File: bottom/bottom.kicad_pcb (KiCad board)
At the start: 2 copper layers, 27.5 x 37.7 mm, 0 parts

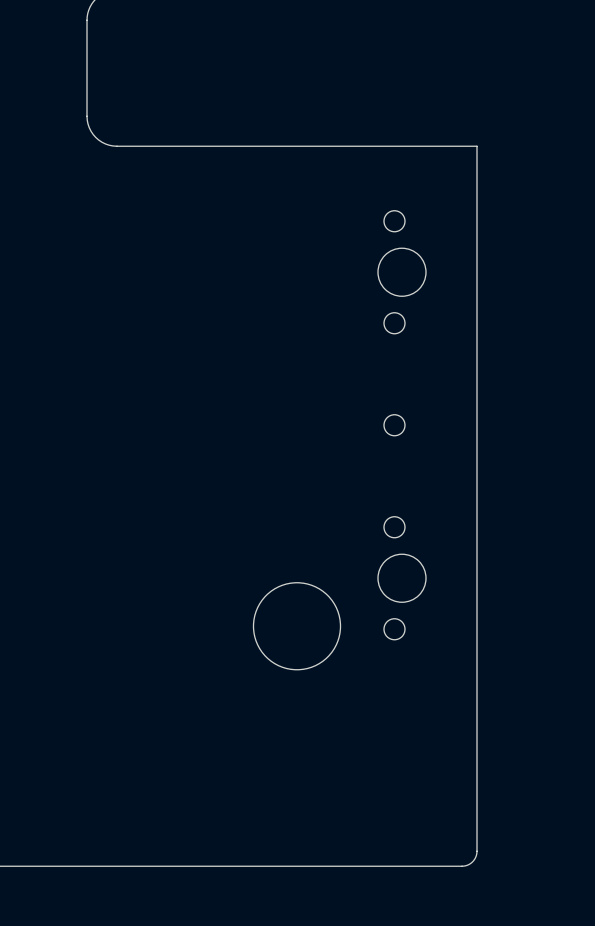
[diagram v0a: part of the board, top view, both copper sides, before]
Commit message: Add pogo pin connector.
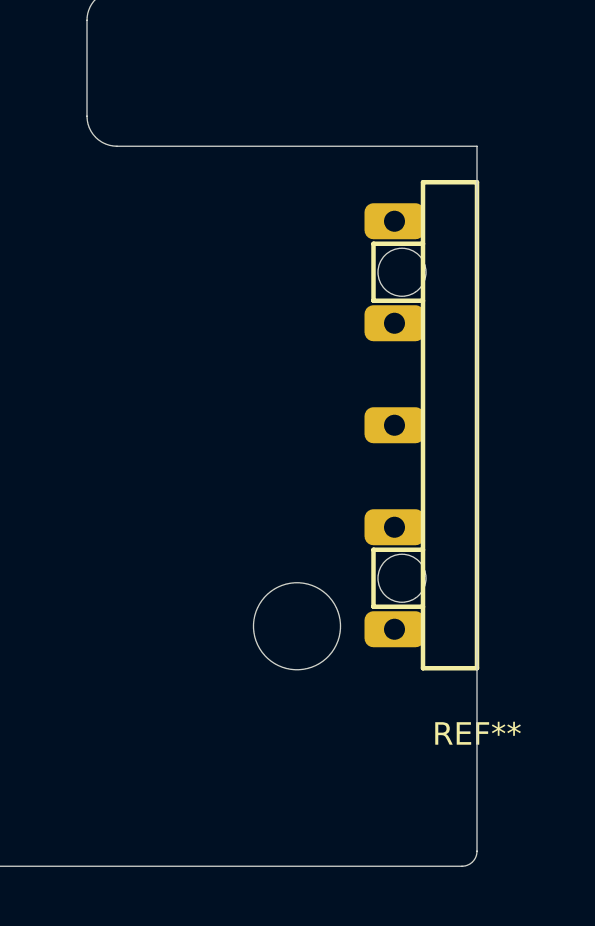
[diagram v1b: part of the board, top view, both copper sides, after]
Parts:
- added REF**: VAL**, ugl:UHK_Male_Pogo_Pin_v2, F.Cu at (225.3, 143.1)
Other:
- outline, holes or cut-outs redrawn
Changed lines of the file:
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@@
   (general
     (thickness 1.6)
-    (drawings 39)
+    (drawings 32)
     (tracks 0)
     (zones 0)
-    (modules 0)
+    (modules 1)
     (nets 1)
   )
@@
     (uvia_drill 0.127)
   )
+  (module ugl:UHK_Male_Pogo_Pin_v2 (layer F.Cu)
+    (at 225.35 143.139999)
+    (attr virtual)
+    (fp_text reference REF** (at 0 10.3) (layer F.SilkS)
+      (effects (font (size 0.75 0.75) (thickness 0.15)))
+    )
+    (fp_text value VAL** (at 0 -9.95 180) (layer F.SilkS) hide
+      (effects (font (size 0.75 0.75) (thickness 0.15)))
+    )
+    (fp_line (start 2.5 -9.1) (end 2.5 9.3) (layer Cmts.User) (width 0.15))
+    (fp_line (start 0 9.3) (end 2.5 9.3) (layer Cmts.User) (width 0.15))
+    (fp_line (start -1.8 8.1) (end -1.8 -8.1) (layer F.SilkS) (width 0.15))
+    (fp_line (start 0 -9.1) (end 2.5 -9.1) (layer Cmts.User) (width 0.15))
+    (fp_line (start 2.5 -7.3) (end 3 -7.3) (layer Cmts.User) (width 0.15))
+    (fp_line (start 2.5 -6.3) (end 3 -6.3) (layer Cmts.User) (width 0.15))
+    (fp_arc (start 3.1 -6.8) (end 3.1 -6.3) (angle -180) (layer Cmts.User) (width 0.15))
+    (fp_line (start 2.5 -2.9) (end 3 -2.9) (layer Cmts.User) (width 0.15))
+    (fp_line (start 2.5 -3.9) (end 3 -3.9) (layer Cmts.User) (width 0.15))
+    (fp_arc (start 3.1 -3.4) (end 3.1 -2.9) (angle -180) (layer Cmts.User) (width 0.15))
+    (fp_line (start 2.5 0.5) (end 3 0.5) (layer Cmts.User) (width 0.15))
+    (fp_line (start 2.5 -0.5) (end 3 -0.5) (layer Cmts.User) (width 0.15))
+    (fp_arc (start 3.1 0) (end 3.1 0.5) (angle -180) (layer Cmts.User) (width 0.15))
+    (fp_line (start 2.5 3.9) (end 3 3.9) (layer Cmts.User) (width 0.15))
+    (fp_line (start 2.5 2.9) (end 3 2.9) (layer Cmts.User) (width 0.15))
+    (fp_arc (start 3.1 3.4) (end 3.1 3.9) (angle -180) (layer Cmts.User) (width 0.15))
+    (fp_line (start 2.5 7.3) (end 3 7.3) (layer Cmts.User) (width 0.15))
+    (fp_line (start 2.5 6.3) (end 3 6.3) (layer Cmts.User) (width 0.15))
+    (fp_arc (start 3.1 6.8) (end 3.1 7.3) (angle -180) (layer Cmts.User) (width 0.15))
+    (fp_line (start 0 9.3) (end 0 -9.1) (layer Cmts.User) (width 0.15))
+    (fp_line (start -1.8 -8.1) (end 0 -8.1) (layer F.SilkS) (width 0.15))
+    (fp_line (start 0 8.1) (end -1.8 8.1) (layer F.SilkS) (width 0.15))
+    (fp_line (start -1.8 -6.05) (end -3.45 -6.05) (layer F.SilkS) (width 0.15))
+    (fp_line (start -3.45 -6.05) (end -3.45 -4.15) (layer F.SilkS) (width 0.15))
+    (fp_line (start -3.45 -4.15) (end -1.8 -4.15) (layer F.SilkS) (width 0.15))
+    (fp_line (start -1.8 6.05) (end -3.45 6.05) (layer F.SilkS) (width 0.15))
+    (fp_line (start -3.45 6.05) (end -3.45 4.15) (layer F.SilkS) (width 0.15))
+    (fp_line (start -3.45 4.15) (end -1.8 4.15) (layer F.SilkS) (width 0.15))
+    (fp_line (start 0 8.1) (end 0 -8.1) (layer F.SilkS) (width 0.15))
+    (pad 1 thru_hole roundrect (at -2.75 -6.8) (size 2 1.2) (drill 0.7) (layers *.Cu *.Mask) (roundrect_rratio 0.25)
+      (clearance 0.0762))
+    (pad 2 thru_hole roundrect (at -2.75 -3.4) (size 2 1.2) (drill 0.7) (layers *.Cu *.Mask) (roundrect_rratio 0.25)
+      (clearance 0.0762))
+    (pad 3 thru_hole roundrect (at -2.75 0) (size 2 1.2) (drill 0.7) (layers *.Cu *.Mask) (roundrect_rratio 0.25))
+    (pad 4 thru_hole roundrect (at -2.75 3.4) (size 2 1.2) (drill 0.7) (layers *.Cu *.Mask) (roundrect_rratio 0.25)
+      (clearance 0.0762))
+    (pad 5 thru_hole roundrect (at -2.75 6.8) (size 2 1.2) (drill 0.7) (layers *.Cu *.Mask) (roundrect_rratio 0.25)
+      (clearance 0.0762))
+    (pad "" np_thru_hole circle (at -2.5 -5.1) (size 1.6 1.6) (drill 1.6) (layers *.Cu *.Mask)
+      (clearance 0.00254))
+    (pad "" np_thru_hole circle (at -2.5 5.1 180) (size 1.6 1.6) (drill 1.6) (layers *.Cu *.Mask)
+      (clearance 0.00254))
+  )
   (gr_circle (center 219.35 149.839996) (end 221 149.839996) (layer Eco1.User) (width 0.01))
   (gr_circle (center 219.35 149.839996) (end 219.35 151.289996) (layer Edge.Cuts) (width 0.01))
@@
   (gr_circle (center 223.35 125.660004) (end 225 125.660004) (layer Eco1.User) (width 0.01))
   (gr_circle (center 223.35 125.660004) (end 223.35 127.110004) (layer Edge.Cuts) (width 0.01))
-  (gr_circle (center 222.85 138.039993) (end 222.85 138.839993) (layer Edge.Cuts) (width 0.01))
-  (gr_circle (center 222.6 146.539993) (end 222.6 146.889993) (layer Edge.Cuts) (width 0.01))
-  (gr_circle (center 222.6 139.740005) (end 222.6 140.090005) (layer Edge.Cuts) (width 0.01))
-  (gr_circle (center 222.6 136.339996) (end 222.6 136.689996) (layer Edge.Cuts) (width 0.01))
-  (gr_circle (center 222.6 143.139999) (end 222.6 143.489999) (layer Edge.Cuts) (width 0.01))
-  (gr_circle (center 222.6 149.940002) (end 222.6 150.290002) (layer Edge.Cuts) (width 0.01))
-  (gr_circle (center 222.85 148.240005) (end 222.85 149.040006) (layer Edge.Cuts) (width 0.01))
   (gr_circle (center 207.85 139.139999) (end 207.85 139.389999) (layer Edge.Cuts) (width 0.01))
   (gr_arc (start 198.35 157.339989) (end 197.85 157.34) (angle -89.98521397) (layer Edge.Cuts) (width 0.01))

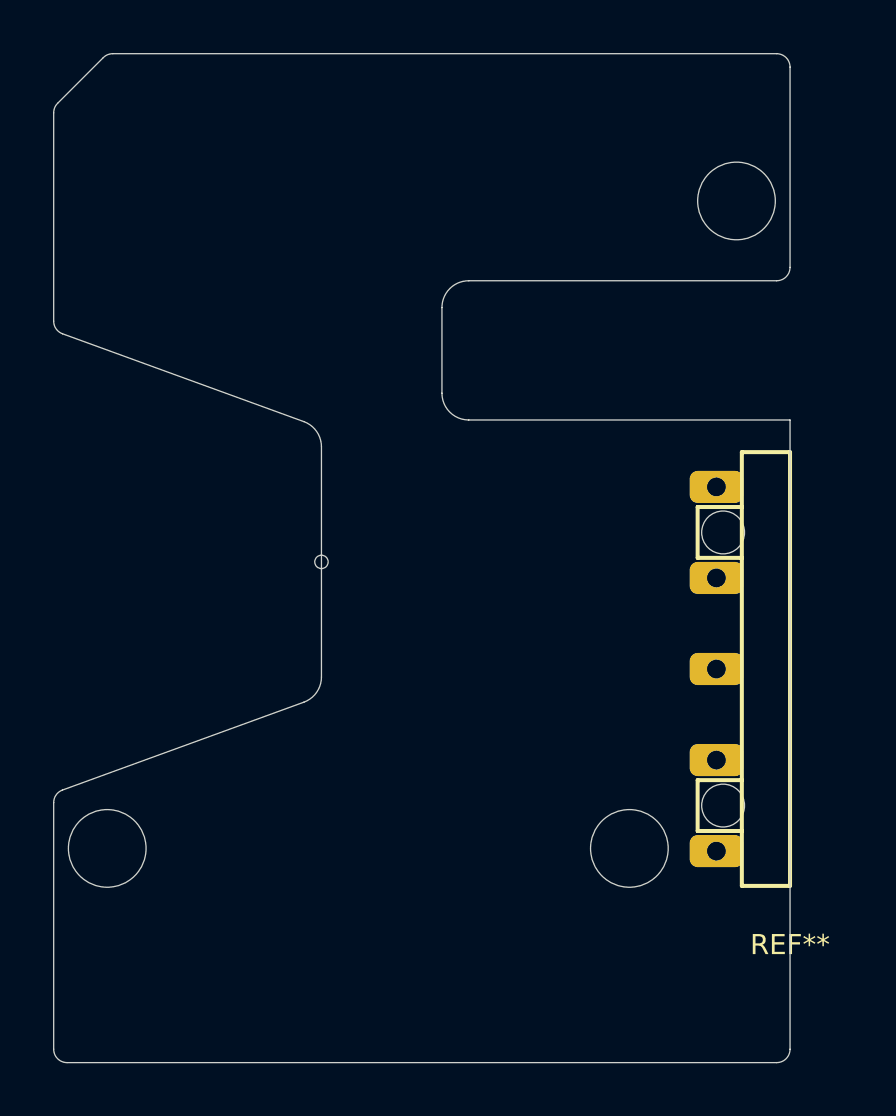
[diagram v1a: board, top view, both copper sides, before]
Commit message: Add FFC connector on the bottom board.
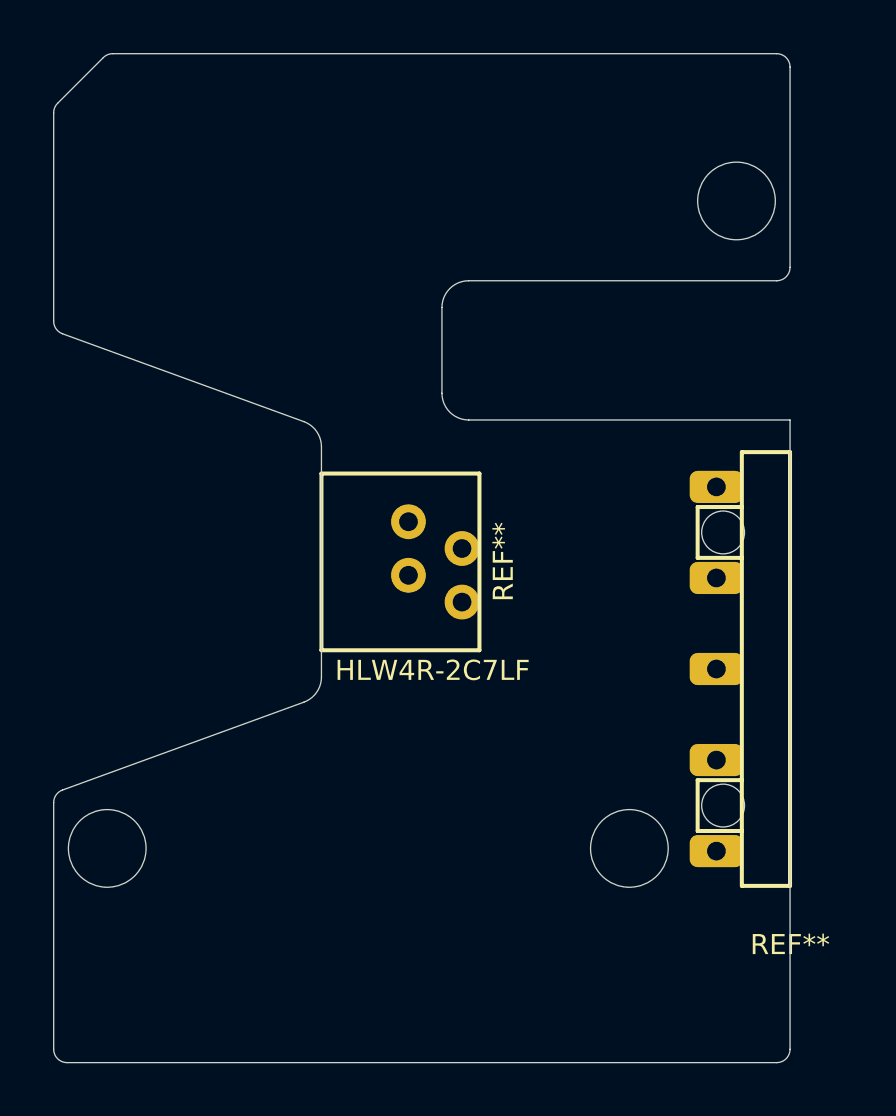
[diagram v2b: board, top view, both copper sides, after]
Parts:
- added REF**: HLW4R-2C7LF, ugl:HLW4R-2C7LF, F.Cu at (207.8, 139.1)
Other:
- outline, holes or cut-outs redrawn
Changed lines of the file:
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@@
   (general
     (thickness 1.6)
-    (drawings 32)
+    (drawings 31)
     (tracks 0)
     (zones 0)
-    (modules 1)
+    (modules 2)
     (nets 1)
   )
@@
     (uvia_drill 0.127)
   )
+  (module ugl:HLW4R-2C7LF (layer F.Cu)
+    (at 207.85 139.139999 270)
+    (descr "FFC connector")
+    (fp_text reference REF** (at 0 -6.8 90) (layer F.SilkS)
+      (effects (font (size 0.75 0.75) (thickness 0.15)))
+    )
+    (fp_text value HLW4R-2C7LF (at 4.060001 -4.15 180) (layer F.SilkS)
+      (effects (font (size 0.75 0.75) (thickness 0.15)))
+    )
+    (fp_line (start -3.3 -5.9) (end 3.3 -5.9) (layer F.SilkS) (width 0.15))
+    (fp_line (start 3.3 0) (end 3.3 -5.9) (layer F.SilkS) (width 0.15))
+    (fp_line (start -3.3 0) (end -3.3 -5.9) (layer F.SilkS) (width 0.15))
+    (fp_line (start -3.3 0) (end 3.3 0) (layer F.SilkS) (width 0.15))
+    (pad 1 thru_hole circle (at 1.5 -5.25 270) (size 1.3 1.3) (drill 0.7) (layers *.Cu *.Mask))
+    (pad 2 thru_hole circle (at 0.5 -3.25 270) (size 1.3 1.3) (drill 0.7) (layers *.Cu *.Mask))
+    (pad 3 thru_hole circle (at -0.5 -5.25 270) (size 1.3 1.3) (drill 0.7) (layers *.Cu *.Mask))
+    (pad 4 thru_hole circle (at -1.5 -3.25 270) (size 1.3 1.3) (drill 0.7) (layers *.Cu *.Mask))
+  )
   (module ugl:UHK_Male_Pogo_Pin_v2 (layer F.Cu)
     (at 225.35 143.139999)
@@
   (gr_circle (center 223.35 125.660004) (end 225 125.660004) (layer Eco1.User) (width 0.01))
   (gr_circle (center 223.35 125.660004) (end 223.35 127.110004) (layer Edge.Cuts) (width 0.01))
-  (gr_circle (center 207.85 139.139999) (end 207.85 139.389999) (layer Edge.Cuts) (width 0.01))
   (gr_arc (start 198.35 157.339989) (end 197.85 157.34) (angle -89.98521397) (layer Edge.Cuts) (width 0.01))
   (gr_arc (start 198.349992 148.129806) (end 198.17899 147.65996) (angle -70.01492042) (layer Edge.Cuts) (width 0.01))

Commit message: Add bottom schematic and route bottom board.
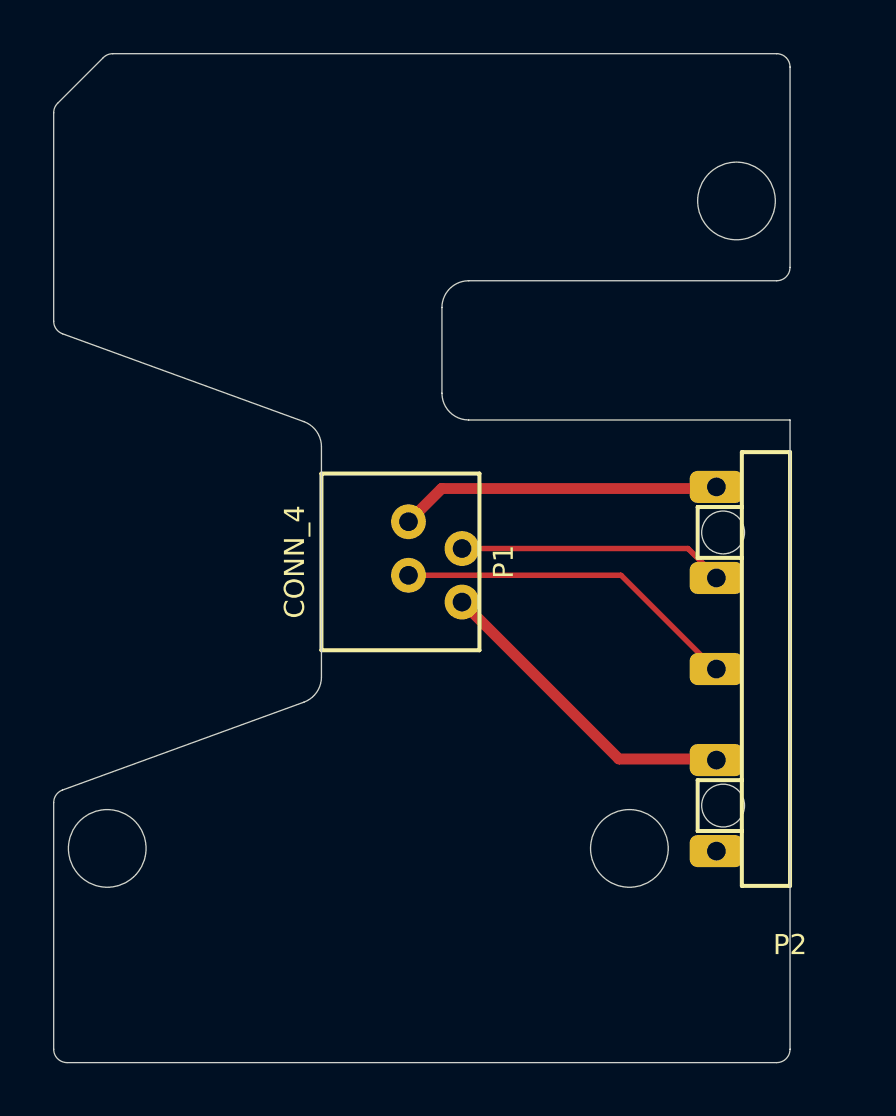
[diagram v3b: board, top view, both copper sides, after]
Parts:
- removed REF**: HLW4R-2C7LF, ugl:HLW4R-2C7LF
- removed REF**: VAL**, ugl:UHK_Male_Pogo_Pin_v2
- added P1: CONN_4, ugl:HLW4R-2C7LF, F.Cu at (207.8, 139.1)
- added P2: CONN_5, ugl:UHK_Male_Pogo_Pin_v2, F.Cu at (225.3, 143.1)
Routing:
- net /SCL: track 0.00 -> 13.0 mm
- net /VCC: track 0.00 -> 12.0 mm
- net /GND: track 0.00 -> 11.9 mm
- net /SDA: track 0.00 -> 9.94 mm
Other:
- net class Default: clearance 0.254 -> 0.2032; trace_width 0.254 -> 0.2032
- rule trace_clearance: 0.254 -> 0.2032
- rule trace_min: 0.254 -> 0.2032

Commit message: Improve silk screen.
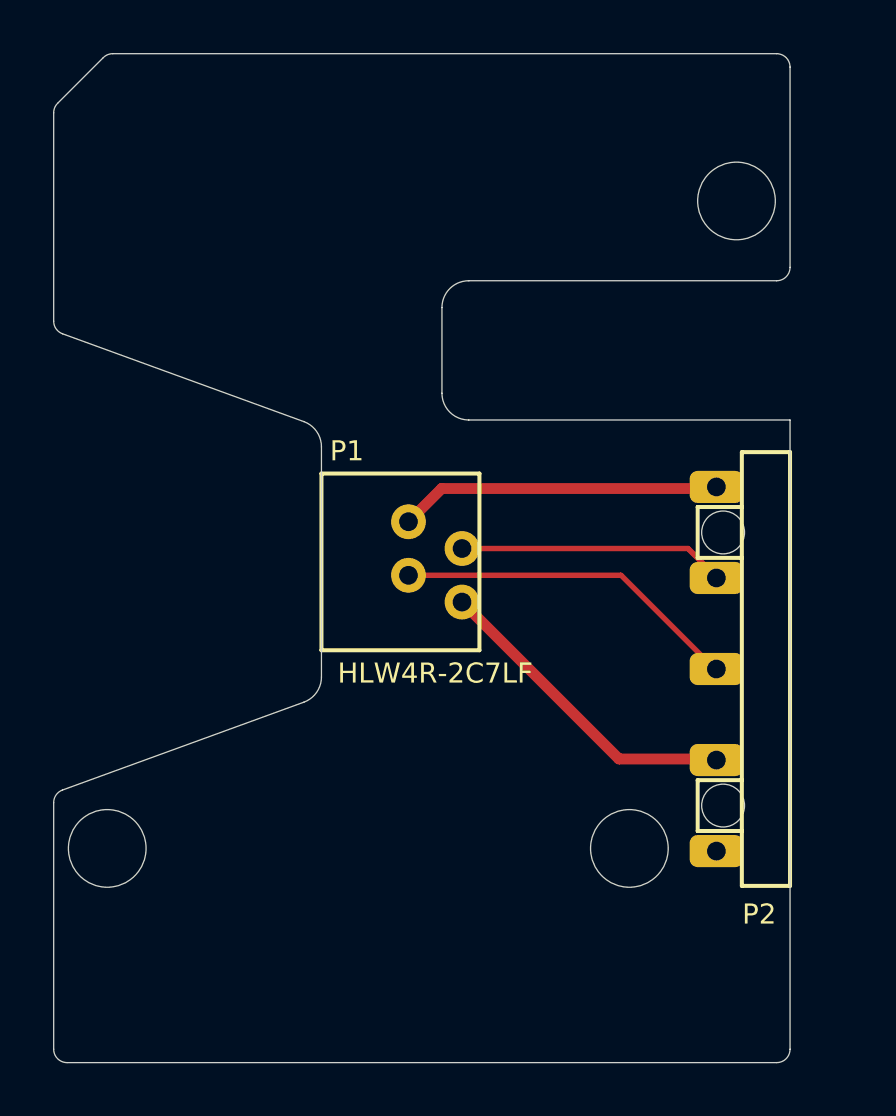
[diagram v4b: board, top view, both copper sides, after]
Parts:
- P1: value CONN_4 -> HLW4R-2C7LF
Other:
- board text added: "PCB ID: touchpad_bottom_1.0.0"
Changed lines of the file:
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@@
   (general
     (thickness 1.6)
-    (drawings 31)
+    (drawings 32)
     (tracks 8)
     (zones 0)
@@
   (title_block
     (title "UHK Touchpad - Bottom")
-    (rev 0.1.0)
+    (rev 1.0.0)
     (company "Ultimate Gadget Laboratories Kft.")
   )
@@
   )
   (setup
-    (last_trace_width 0.4064)
+    (last_trace_width 0.2032)
     (user_trace_width 0.4064)
     (trace_clearance 0.2032)
@@
     (pcb_text_size 1.5 1.5)
     (mod_edge_width 0.15)
-    (mod_text_size 1 1)
+    (mod_text_size 0.75 0.75)
     (mod_text_width 0.15)
     (pad_size 1.5 1.5)
@@
     (at 207.85 139.139999 270)
     (descr "FFC connector")
-    (fp_text reference P1 (at 0 -6.8 90) (layer F.SilkS)
+    (fp_text reference P1 (at -4.139999 -0.95 180) (layer F.SilkS)
       (effects (font (size 0.75 0.75) (thickness 0.15)))
     )
-    (fp_text value CONN_4 (at 0 1 90) (layer F.SilkS)
+    (fp_text value HLW4R-2C7LF (at 4.160001 -4.25 180) (layer F.SilkS)
       (effects (font (size 0.75 0.75) (thickness 0.15)))
     )
@@
     (at 225.35 143.139999)
     (attr virtual)
-    (fp_text reference P2 (at 0 10.3) (layer F.SilkS)
+    (fp_text reference P2 (at -1.15 9.160001) (layer F.SilkS)
       (effects (font (size 0.75 0.75) (thickness 0.15)))
     )
@@
       (net 1 /VCC) (clearance 0.0762))
   )
+  (gr_text "PCB ID: touchpad_bottom_1.0.0" (at 212 156.8) (layer B.SilkS)
+    (effects (font (size 0.75 0.75) (thickness 0.15)) (justify mirror))
+  )
   (gr_circle (center 219.35 149.839996) (end 221 149.839996) (layer Eco1.User) (width 0.01))
